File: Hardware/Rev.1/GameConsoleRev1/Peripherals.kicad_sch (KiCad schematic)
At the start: 1 part, among them J15 Conn_01x09_Pin

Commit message: A
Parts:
- J15: footprint (none) -> Connector_PinSocket_2.54mm:PinSocket_1x11_P2.54mm_Vertical; symbol Connector:Conn_01x09_Pin -> Connector:Conn_01x11_Pin
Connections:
- net GPIO11: now also J15.2 (Pin_2); no longer J15.1 (Pin_1)
- net GPIO30: now also J15.3 (Pin_3); no longer J15.2 (Pin_2)
- net GPIO31: now also J15.4 (Pin_4); no longer J15.3 (Pin_3)
- net GPIO36: now also J15.5 (Pin_5); no longer J15.4 (Pin_4)
- net GPIO37: now also J15.6 (Pin_6); no longer J15.5 (Pin_5)
- net GPIO38: now also J15.7 (Pin_7); no longer J15.6 (Pin_6)
- net GPIO39: now also J15.8 (Pin_8); no longer J15.7 (Pin_7)
- net GPIO46: now also J15.9 (Pin_9); no longer J15.8 (Pin_8)
- net GPIO47: now also J15.10 (Pin_10); no longer J15.9 (Pin_9)
- new net +3V3: J15.1 (Pin_1)
- new net GND: J15.11 (Pin_11)
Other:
- added sheet LEDs (leds.kicad_sch)

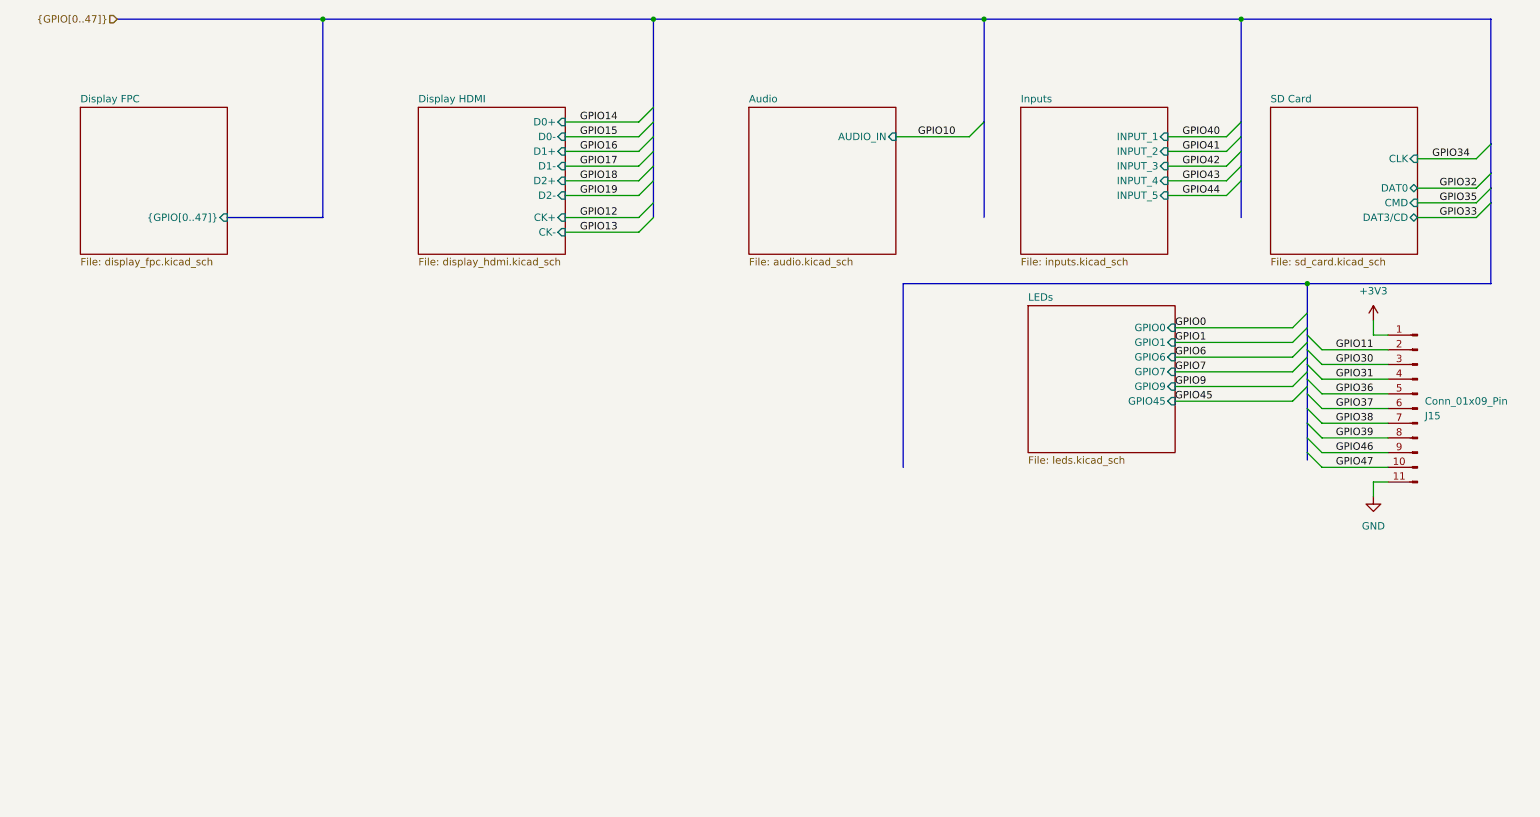
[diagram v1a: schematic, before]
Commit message: Added CPP Build
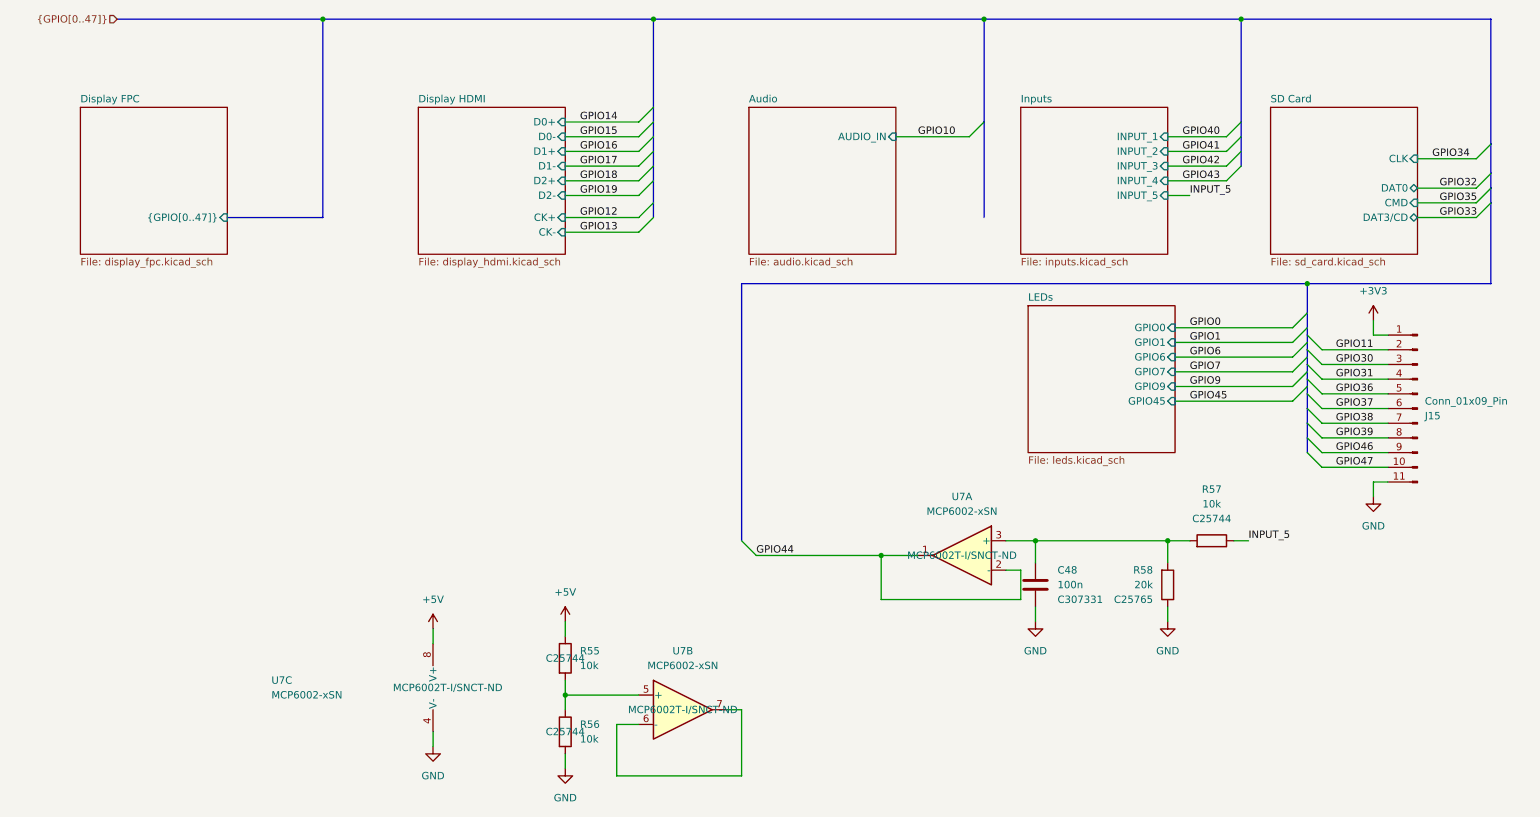
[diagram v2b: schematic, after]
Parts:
- added C48: 100n, Capacitor_SMD:C_0402_1005Metric, symbol Device:C
- added R55, R56, R57: 10k, Resistor_SMD:R_0402_1005Metric, symbol Device:R
- added R58: 20k, Resistor_SMD:R_0402_1005Metric, symbol Device:R
- added U7: MCP6002-xSN, Package_SO:SOIC-8_3.9x4.9mm_P1.27mm, symbol Amplifier_Operational:MCP6002-xSN
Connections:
- net GND: now also C48.1, R56.2, R58.1, U7.4 (V-)
- net GPIO44: now also U7.1, U7.2 (-)
- new net: C48.2, R57.2, R58.2, U7.3 (+)
- new net: R55.2, R56.1, U7.5 (+)
- new net: U7.6 (-), U7.7
- new net +5V: R55.1, U7.8 (V+)
- new net INPUT_5: R57.1
